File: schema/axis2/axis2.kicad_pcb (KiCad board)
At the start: 2 copper layers, 69 x 110 mm, 16 parts, among them J1 JA, J2 JB, J3 5VPower, J4 12VPower, J5 Power Motor 1, J6 Power Motor 2, J7 M1, J8 M2, J9 RC-PPM, U1 gy-9250, U2 L7805, U3 axis2-frame

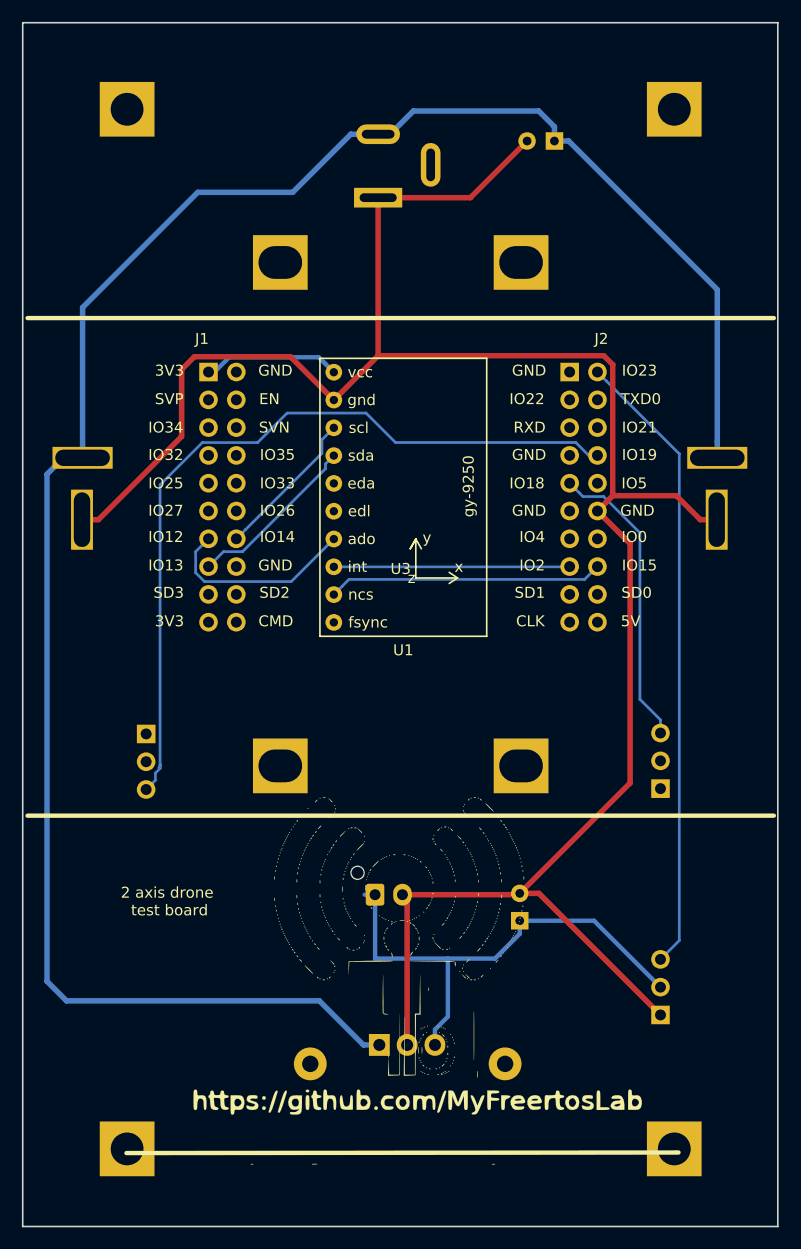
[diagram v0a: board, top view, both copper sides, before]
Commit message: Corretto scheda e testato relay per switch on/off motori. Implementato ciclo di switch on/off motori
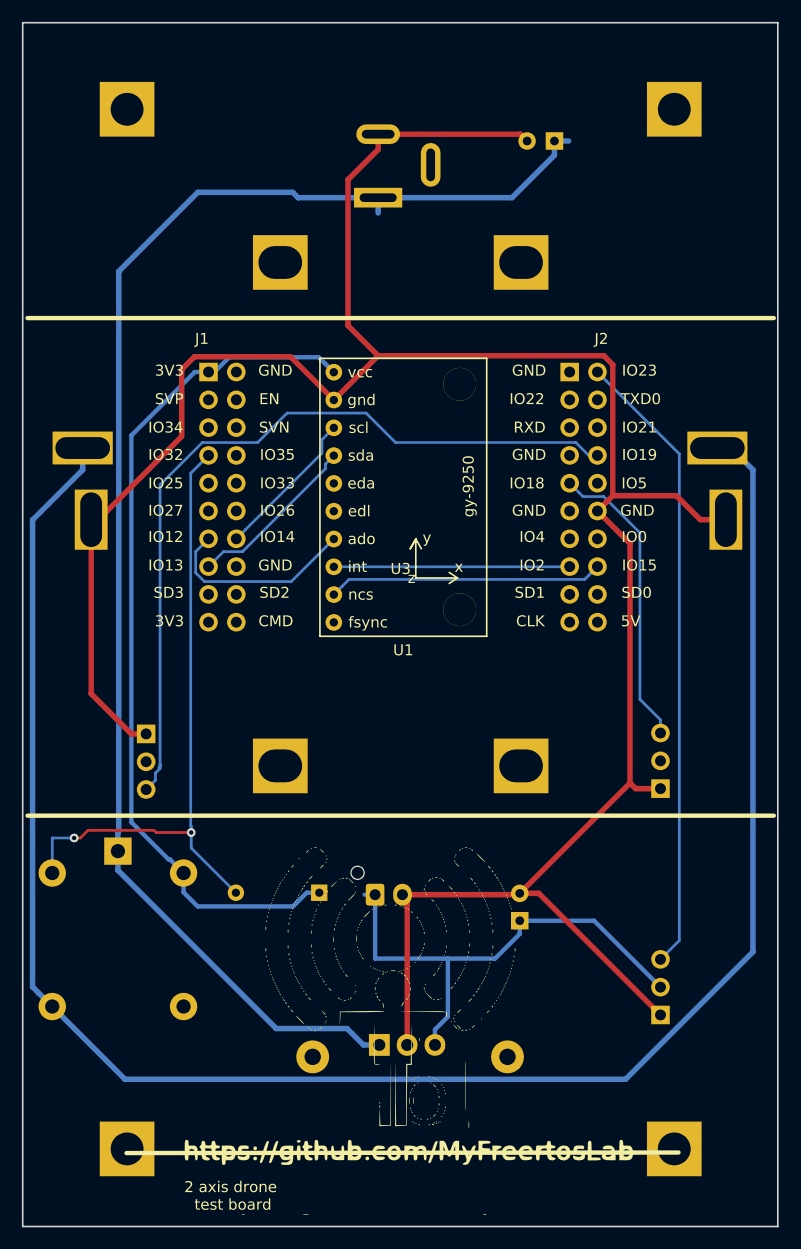
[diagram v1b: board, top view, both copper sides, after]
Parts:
- added D1: D_ALT, Diode_THT:D_DO-34_SOD68_P7.62mm_Horizontal, B.Cu at (106.1, 129.5)
- added RLY1: G5LE-14_DC5, Relay_THT:Relay_SPDT_Omron-G5LE-1, B.Cu at (87.7, 125.7)
- moved G*** 4.67 mm to (114.3, 142.1)
- moved HS1 0.68 mm to (114.4, 144.5)
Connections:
- J1 pad 7: Net-(J1-Pad7) -> GPIO32
- J4 pad 1: GND -> +12V
- J4 pad 2: +12V -> GND
- J5 pad 1: +12V -> +12VM
- J6 pad 1: +12V -> +12VM
- J7 pad 1: Net-(J7-Pad1) -> GND
- J8 pad 1: Net-(J8-Pad1) -> GND
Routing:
- net +12VM: track 0.00 -> 175.2 mm
- net +3V3: track 12.6 -> 79.3 mm
- net GPIO32: track 0.00 -> 58.6 mm, vias 0 -> 2
- net +12V: track 185.0 -> 133.9 mm
- net GND: track 199.0 -> 231.7 mm

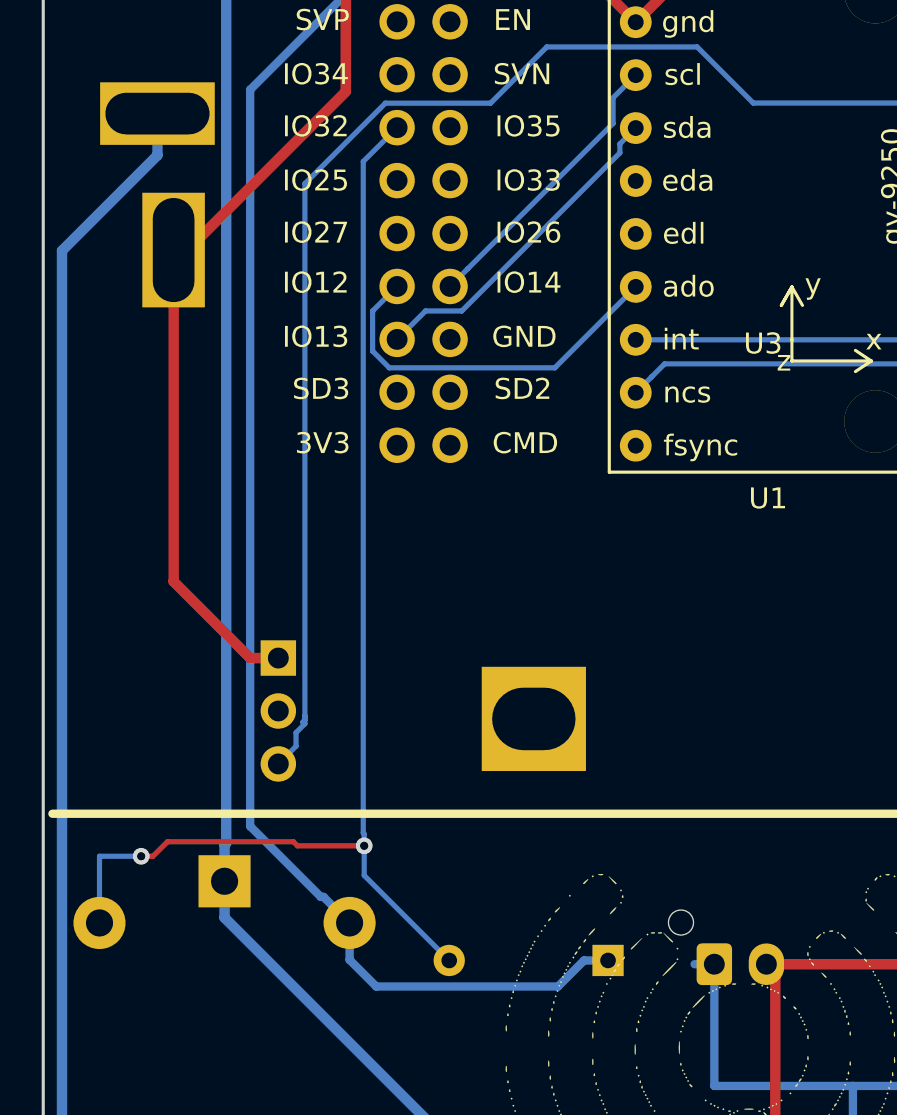
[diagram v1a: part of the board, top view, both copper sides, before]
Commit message: Modificato scheda aggiungendo BC547.
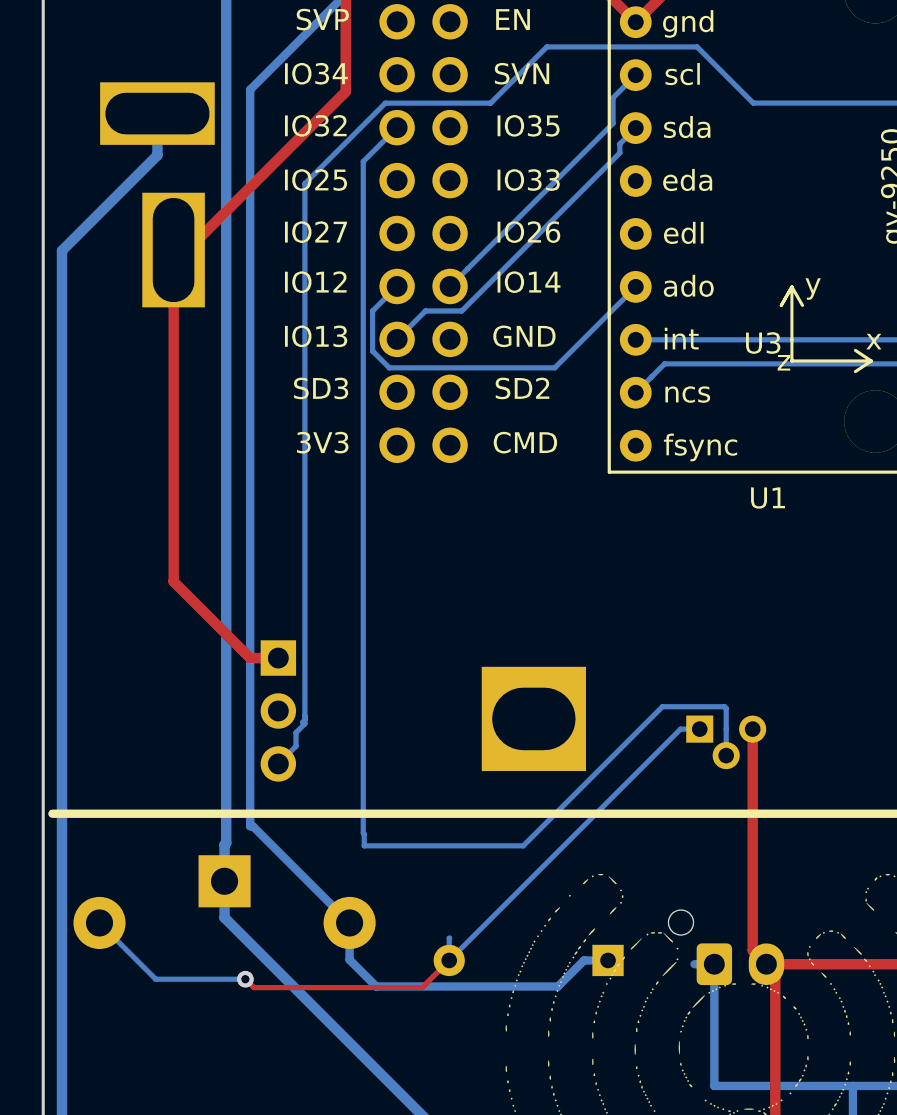
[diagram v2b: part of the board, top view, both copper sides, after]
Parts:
- added Q1: BC547, Package_TO_SOT_THT:TO-92, B.Cu at (110.5, 118.4)
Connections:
- D1 pad 2: GPIO32 -> Net-(D1-Pad2)
- RLY1 pad 5: GPIO32 -> Net-(D1-Pad2)
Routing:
- net Net-(D1-Pad2): track 0.00 -> 36.3 mm, vias 0 -> 1
- net GND: track 231.7 -> 243.2 mm
- net GPIO32: track 58.6 -> 57.6 mm, vias 2 -> 0
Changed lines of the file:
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@@
     (thickness 1.6)
     (drawings 84)
-    (tracks 154)
+    (tracks 161)
     (zones 0)
-    (modules 18)
-    (nets 52)
+    (modules 19)
+    (nets 53)
   )
   (page A4)
@@
   (net 50 +12VM)
   (net 51 "Net-(RLY1-Pad3)")
+  (net 52 "Net-(D1-Pad2)")
   (net_class Default "This is the default net class."
     (clearance 0.2)
@@
     (add_net MOSI)
     (add_net NCS)
+    (add_net "Net-(D1-Pad2)")
     (add_net "Net-(HS1-Pad1)")
     (add_net "Net-(HS1-Pad2)")
@@
       (net 36 +3V3))
     (pad 2 thru_hole oval (at 7.62 0 180) (size 1.5 1.5) (drill 0.75) (layers *.Cu *.Mask)
-      (net 49 GPIO32))
+      (net 52 "Net-(D1-Pad2)"))
     (model ${KISYS3DMOD}/Diode_THT.3dshapes/D_DO-34_SOD68_P7.62mm_Horizontal.wrl
       (at (xyz 0 0 0))
@@
       (net 50 +12VM))
     (pad 5 thru_hole oval (at 6 -2 180) (size 2.5 2.5) (drill 1.3) (layers *.Cu *.Mask)
-      (net 49 GPIO32))
+      (net 52 "Net-(D1-Pad2)"))
     (model ${KISYS3DMOD}/Relay_THT.3dshapes/Relay_SPDT_Omron-G5LE-1.wrl
       (at (xyz 0 0 0))
@@
     )
   )
+  (module Package_TO_SOT_THT:TO-92 (layer B.Cu)
+    (at 110.5 118.4)
+    (descr "TO-92 leads molded, narrow, drill 0.75mm (see NXP sot054_po.pdf)")
+    (tags "to-92 sc-43 sc-43a sot54 PA33 transistor")
+    (fp_text reference Q1 (at 1.27 3.56) (layer B.SilkS)
+      (effects (font (size 1 1) (thickness 0.15)) (justify mirror))
+    )
+    (fp_text value BC547 (at 1.27 -2.79) (layer B.Fab)
+      (effects (font (size 1 1) (thickness 0.15)) (justify mirror))
+    )
+    (fp_text user %R (at 1.27 0) (layer B.Fab)
+      (effects (font (size 1 1) (thickness 0.15)) (justify mirror))
+    )
+    (fp_line (start -0.53 -1.85) (end 3.07 -1.85) (layer B.SilkS) (width 0.12))
+    (fp_line (start -0.5 -1.75) (end 3 -1.75) (layer B.Fab) (width 0.1))
+    (fp_line (start -1.46 2.73) (end 4 2.73) (layer B.CrtYd) (width 0.05))
+    (fp_line (start -1.46 2.73) (end -1.46 -2.01) (layer B.CrtYd) (width 0.05))
+    (fp_line (start 4 -2.01) (end 4 2.73) (layer B.CrtYd) (width 0.05))
+    (fp_line (start 4 -2.01) (end -1.46 -2.01) (layer B.CrtYd) (width 0.05))
+    (fp_arc (start 1.27 0) (end 1.27 2.48) (angle -135) (layer B.Fab) (width 0.1))
+    (fp_arc (start 1.27 0) (end 1.27 2.6) (angle 135) (layer B.SilkS) (width 0.12))
+    (fp_arc (start 1.27 0) (end 1.27 2.48) (angle 135) (layer B.Fab) (width 0.1))
+    (fp_arc (start 1.27 0) (end 1.27 2.6) (angle -135) (layer B.SilkS) (width 0.12))
+    (pad 2 thru_hole circle (at 1.27 1.27) (size 1.3 1.3) (drill 0.75) (layers *.Cu *.Mask)
+      (net 49 GPIO32))
+    (pad 3 thru_hole circle (at 2.54 0) (size 1.3 1.3) (drill 0.75) (layers *.Cu *.Mask)
+      (net 34 GND))
+    (pad 1 thru_hole rect (at 0 0) (size 1.3 1.3) (drill 0.75) (layers *.Cu *.Mask)
+      (net 52 "Net-(D1-Pad2)"))
+    (model ${KISYS3DMOD}/Package_TO_SOT_THT.3dshapes/TO-92.wrl
+      (at (xyz 0 0 0))
+      (scale (xyz 1 1 1))
+      (rotate (xyz 0 0 0))
+    )
+  )
   (gr_text "2 axis drone\n test board" (at 98 157.2) (layer F.SilkS)
     (effects (font (size 1 1) (thickness 0.2)))
@@
   (segment (start 135.01 119.99) (end 137.28 119.99) (width 0.5) (layer F.Cu) (net 34))
   (segment (start 134.5 119.48) (end 135.01 119.99) (width 0.5) (layer F.Cu) (net 34))
-  (segment (start 110.25 129.68) (end 111.2 129.68) (width 0.4) (layer B.Cu) (net 35))
+  (segment (start 113.04 129.02) (end 113.7 129.68) (width 0.5) (layer F.Cu) (net 34))
+  (segment (start 113.04 118.4) (end 113.04 129.02) (width 0.5) (layer F.Cu) (net 34))
   (segment (start 122.16 135.52) (end 124.42 133.26) (width 0.4) (layer B.Cu) (net 35))
   (segment (start 124.42 133.26) (end 124.42 132.06) (width 0.4) (layer B.Cu) (net 35))
@@
   (segment (start 131.209852 132.06) (end 124.42 132.06) (width 0.4) (layer B.Cu) (net 35))
   (segment (start 137.28 138.130148) (end 131.209852 132.06) (width 0.4) (layer B.Cu) (net 35))
+  (segment (start 110.25 129.68) (end 111.2 129.68) (width 0.4) (layer B.Cu) (net 35))
   (segment (start 106.668001 81.178001) (end 107.43 81.94) (width 0.4) (layer B.Cu) (net 36))
   (segment (start 106.059999 80.569999) (end 106.668001 81.178001) (width 0.4) (layer B.Cu) (net 36))
@@
   (segment (start 88.929999 123.062001) (end 88.929999 87.720001) (width 0.4) (layer B.Cu) (net 36))
   (segment (start 94.73 81.92) (end 95.98 81.92) (width 0.4) (layer B.Cu) (net 36))
-  (segment (start 92.450001 126.450001) (end 93.7 127.7) (width 0.4) (layer B.Cu) (net 36))
-  (segment (start 92.317999 126.450001) (end 92.450001 126.450001) (width 0.4) (layer B.Cu) (net 36))
-  (segment (start 88.929999 123.062001) (end 92.317999 126.450001) (width 0.4) (layer B.Cu) (net 36))
   (segment (start 103.699999 130.750001) (end 104.95 129.5) (width 0.4) (layer B.Cu) (net 36))
   (segment (start 94.982235 130.750001) (end 103.699999 130.750001) (width 0.4) (layer B.Cu) (net 36))
@@
   (segment (start 93.7 129.467766) (end 94.982235 130.750001) (width 0.4) (layer B.Cu) (net 36))
   (segment (start 93.7 127.7) (end 93.7 129.467766) (width 0.4) (layer B.Cu) (net 36))
+  (segment (start 89.062001 123.062001) (end 93.7 127.7) (width 0.4) (layer B.Cu) (net 36))
+  (segment (start 88.929999 123.062001) (end 89.062001 123.062001) (width 0.4) (layer B.Cu) (net 36))
   (segment (start 103.545001 101.064999) (end 107.43 97.18) (width 0.25) (layer B.Cu) (net 37))
   (segment (start 95.98 97.16) (end 94.804999 98.335001) (width 0.25) (layer B.Cu) (net 37))
@@
   (segment (start 139 133.870148) (end 139 89.4) (width 0.25) (layer B.Cu) (net 46))
   (segment (start 137.28 135.590148) (end 139 133.870148) (width 0.25) (layer B.Cu) (net 46))
-  (segment (start 81.7 127.7) (end 81.7 124.5) (width 0.25) (layer B.Cu) (net 49))
-  (segment (start 81.7 124.5) (end 83.7 124.5) (width 0.25) (layer B.Cu) (net 49))
-  (segment (start 83.7 124.5) (end 83.7 124.5) (width 0.25) (layer B.Cu) (net 49))
-  (via (at 83.7 124.5) (size 0.8) (drill 0.4) (layers F.Cu B.Cu) (net 49))
-  (segment (start 84.265685 124.5) (end 84.965685 123.8) (width 0.25) (layer F.Cu) (net 49))
-  (segment (start 83.7 124.5) (end 84.265685 124.5) (width 0.25) (layer F.Cu) (net 49))
-  (segment (start 84.965685 123.8) (end 91 123.8) (width 0.25) (layer F.Cu) (net 49))
-  (via (at 94.4 124) (size 0.8) (drill 0.4) (layers F.Cu B.Cu) (net 49))
-  (segment (start 91.2 124) (end 94.4 124) (width 0.25) (layer F.Cu) (net 49))
-  (segment (start 91 123.8) (end 91.2 124) (width 0.25) (layer F.Cu) (net 49))
-  (segment (start 94.4 125.42) (end 94.4 124) (width 0.25) (layer B.Cu) (net 49))
-  (segment (start 98.48 129.5) (end 94.4 125.42) (width 0.25) (layer B.Cu) (net 49))
-  (segment (start 94.354989 123.389304) (end 94.354989 91.165011) (width 0.25) (layer B.Cu) (net 49))
-  (segment (start 94.354989 91.165011) (end 95.98 89.54) (width 0.25) (layer B.Cu) (net 49))
-  (segment (start 94.4 123.434315) (end 94.354989 123.389304) (width 0.25) (layer B.Cu) (net 49))
-  (segment (start 94.4 124) (end 94.4 123.434315) (width 0.25) (layer B.Cu) (net 49))
+  (segment (start 111.77 117.4) (end 111.77 118.4) (width 0.25) (layer B.Cu) (net 49))
+  (segment (start 111.694999 117.324999) (end 111.77 117.4) (width 0.25) (layer B.Cu) (net 49))
+  (segment (start 108.710003 117.324999) (end 111.694999 117.324999) (width 0.25) (layer B.Cu) (net 49))
+  (segment (start 102.035002 124) (end 108.710003 117.324999) (width 0.25) (layer B.Cu) (net 49))
+  (segment (start 94.4 124) (end 102.035002 124) (width 0.25) (layer B.Cu) (net 49))
+  (segment (start 95.98 89.54) (end 94.354989 91.165011) (width 0.25) (layer B.Cu) (net 49))
+  (segment (start 94.354989 91.165011) (end 94.354989 123.389304) (width 0.25) (layer B.Cu) (net 49))
+  (segment (start 94.4 123.434315) (end 94.4 124) (width 0.25) (layer B.Cu) (net 49))
+  (segment (start 94.354989 123.389304) (end 94.4 123.434315) (width 0.25) (layer B.Cu) (net 49))
+  (segment (start 111.77 118.4) (end 111.77 119.67) (width 0.25) (layer B.Cu) (net 49))
   (segment (start 84.4705 89.7609) (end 82.7205 89.7609) (width 0.5) (layer B.Cu) (net 50))
   (segment (start 145.73 134.91015) (end 145.73 90.865) (width 0.5) (layer B.Cu) (net 50))
@@
   (segment (start 84.48 90.865) (end 79.899999 95.445001) (width 0.5) (layer B.Cu) (net 50))
   (segment (start 84.48 88.865) (end 84.48 90.865) (width 0.5) (layer B.Cu) (net 50))
+  (segment (start 109.58 118.4) (end 98.48 129.5) (width 0.25) (layer B.Cu) (net 52))
+  (segment (start 110.5 118.4) (end 109.58 118.4) (width 0.25) (layer B.Cu) (net 52))
+  (segment (start 88.7 130.4) (end 88.7 130.4) (width 0.25) (layer B.Cu) (net 52))
+  (via (at 88.7 130.4) (size 0.8) (drill 0.4) (layers F.Cu B.Cu) (net 52))
+  (segment (start 98.48 128.43934) (end 98.5 128.41934) (width 0.25) (layer B.Cu) (net 52))
+  (segment (start 98.48 129.5) (end 98.48 128.43934) (width 0.25) (layer B.Cu) (net 52))
+  (segment (start 97.730001 130.249999) (end 98.48 129.5) (width 0.25) (layer F.Cu) (net 52))
+  (segment (start 89.099999 130.799999) (end 97.180001 130.799999) (width 0.25) (layer F.Cu) (net 52))
+  (segment (start 97.180001 130.799999) (end 97.730001 130.249999) (width 0.25) (layer F.Cu) (net 52))
+  (segment (start 88.7 130.4) (end 89.099999 130.799999) (width 0.25) (layer F.Cu) (net 52))
+  (segment (start 84.4 130.4) (end 88.7 130.4) (width 0.25) (layer B.Cu) (net 52))
+  (segment (start 81.7 127.7) (end 84.4 130.4) (width 0.25) (layer B.Cu) (net 52))
 )
